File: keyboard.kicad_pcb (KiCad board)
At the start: 2 copper layers, 229.9 x 77.5 mm, 212 parts, among them IC1 ATMEGA32U4, J1 USBMINI_B05, P1 ISP, P2 GPIO Port, Q1 MOS_P, X1 CRYSTAL

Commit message: Final touches on schematic & Clean up PCB
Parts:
- added D321, D331, D381, D41, D42: DIODE, Diodes_SMD:SOD-123, B.Cu at (151.3, 129.9)
- added LED331: LED, mx1a:MX1A-led, F.Cu at (175.3, 143.5)
- added LED341: LED, mx1a:MX1A-led, F.Cu at (146.1, 151.1)
- added LED391: LED, mx1a:MX1A-led, F.Cu at (81.3, 154.9)
- added LED41: LED, mx1a:MX1A-led, F.Cu at (53.3, 170.2)
- added LED42: LED, mx1a:MX1A-led, F.Cu at (199.4, 141.0)
- added LR331, LR341, LR391, LR43: 330R, Resistors_SMD:R_0805, B.Cu at (151.3, 129.9)
- added LR42: 330R, Resistors_SMD:R_0805, B.Cu at (133.3, 130.8)
- added S321: MX1A, mx1a:MX1A, F.Cu at (58.4, 146.1)
- added S331: MX1A, mx1a:MX1A, F.Cu at (108.0, 133.3)
- added S381: MX1A, mx1a:MX1A, F.Cu at (162.6, 165.1)
- added S41: MX1A, mx1a:MX1A, F.Cu at (124.5, 165.1)
- added S42: MX1A, mx1a:MX1A, F.Cu at (94.0, 171.4)
- D1, D10, D11, D12, D13, D14, D15, D16, D17, D18, D19, D2, D20, D21, D22, D23, D24, D25, D26, D27, D28, D29, D3, D30, D31, D32, D33, D34, D35, D36, D37, D38, D39, D4, D40, D5, D6, D7, D8, D9: footprint SM0805:SM0805D -> Diodes_SMD:SOD-123
- IC1: footprint tqfp:TQFP44 -> Housings_QFP:TQFP-44_10x10mm_Pitch0.8mm
- LED1, LED10, LED11, LED12, LED13, LED14, LED15, LED16, LED17, LED18, LED19, LED2, LED20, LED21, LED22, LED23, LED24, LED25, LED26, LED27, LED28, LED29, LED3, LED30, LED31, LED32, LED33, LED34, LED35, LED36, LED37, LED38, LED39, LED4, LED40, LED5, LED6, LED7, LED8, LED9: footprint mx1a-led:MX1A-led -> mx1a:MX1A-led
- S1, S10, S11, S12, S13, S14, S15, S16, S17, S18, S19, S2, S20, S21, S22, S23, S24, S25, S26, S27, S28, S29, S3, S30, S31, S32, S33, S34, S35, S36, S38, S39, S4, S40, S5, S6, S7, S8, S9: footprint MX1A_alps:MX1ALPS -> mx1a:MX1A
- S37: footprint 6.25:CHERRY_PCB_625H_Rev -> mx1a:MX1A
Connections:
- net /Matrix/Col0 renamed /Col0
- net /Matrix/Col1 renamed /Col1
- net /Matrix/Col2 renamed /Col2
- net /Matrix/Col3 renamed /Col3
- net /Matrix/Col6 renamed /Col6
- net /Matrix/Row0 renamed /Row0
- net /Matrix/Row1 renamed /Row1
- net /Matrix/Row2 renamed /Row2
- net /Matrix/Row3 renamed /Row3
- net /led/Backlight renamed /Backlight
- net /led/CapsLock renamed /Caps
- net /led/ESC renamed /ESC
- net /led/WASD renamed /WASD
- D10 pad 1: /Matrix/Col9 -> /Col9
- D11 pad 1: /Matrix/Col10 -> /Col10
- D16 pad 1: /Matrix/Col4 -> /Col4
- D17 pad 1: /Matrix/Col5 -> /Col5
- D19 pad 1: /Matrix/Col7 -> /Col7
- D20 pad 1: /Matrix/Col8 -> /Col8
- D21 pad 1: /Matrix/Col9 -> /Col9
- D22 pad 1: /Matrix/Col10 -> /Col10
- D27 pad 1: /Matrix/Col4 -> /Col4
- D28 pad 1: /Matrix/Col5 -> /Col5
- D30 pad 1: /Matrix/Col7 -> /Col7
- D31 pad 1: /Matrix/Col8 -> /Col8
- D32 pad 1: /Matrix/Col9 -> /Col9
- D33 pad 1: /Matrix/Col10 -> /Col10
- D37 pad 1: /Matrix/Col5 -> /Col4
- D38 pad 1: /Matrix/Col8 -> /Col5
- D39 pad 1: /Matrix/Col9 -> /Col7
- D40 pad 1: /Matrix/Col10 -> /Col8
- D5 pad 1: /Matrix/Col4 -> /Col4
- D6 pad 1: /Matrix/Col5 -> /Col5
- D8 pad 1: /Matrix/Col7 -> /Col7
- D9 pad 1: /Matrix/Col8 -> /Col8
- IC1 pad 12: /Matrix/Col10 -> /Col10
- IC1 pad 28: /Matrix/Col7 -> /Col7
- IC1 pad 29: /Matrix/Col8 -> /Col8
- IC1 pad 30: /Matrix/Col9 -> /Col9
- IC1 pad 32: /led/Bottom -> /Bottom
- IC1 pad 36: /Matrix/Col5 -> /Col5
- IC1 pad 37: /Matrix/Col4 -> /Col4
- LR41 pad 1: Net-(LR41-Pad1) -> /led/LRow0
- LR41 pad 2: /led/Bottom -> Net-(LED41-Pad1)
- RGBLED1 pad 4: Net-(LR41-Pad1) -> Net-(LR43-Pad1)
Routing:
- net GND: track 1231.4 -> 0.00 mm, vias 33 -> 0
- net VCC: track 978.1 -> 0.00 mm, vias 49 -> 0
- net /led/LRow0: track 818.9 -> 0.00 mm, vias 32 -> 0
- net /Row2: track 314.2 -> 0.00 mm, vias 2 -> 0
- net /Row3: track 310.6 -> 0.00 mm, vias 5 -> 0
- net /Row1: track 305.8 -> 0.00 mm, vias 5 -> 0
- net /ESC: track 292.0 -> 0.00 mm, vias 1 -> 0
- net /Matrix/Col10: track 281.1 -> 0.00 mm, vias 9 -> 0
- net /Row0: track 277.7 -> 0.00 mm, vias 2 -> 0
- net /Matrix/Col8: track 235.0 -> 0.00 mm, vias 2 -> 0
- net /Matrix/Col9: track 228.9 -> 0.00 mm, vias 2 -> 0
- net /GPIO2: track 227.9 -> 0.00 mm, vias 6 -> 0
- net /GPIO0: track 206.8 -> 0.00 mm, vias 6 -> 0
- net /GPIO1: track 206.6 -> 0.00 mm, vias 8 -> 0
- net /GPIO3: track 167.0 -> 0.00 mm, vias 3 -> 0
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
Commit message: 旋转跳跃我闭着眼
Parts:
- moved C7 116.7 mm to (255.3, 137.2)
- moved C1 116.6 mm to (255.3, 141.0)
- moved C2 116.6 mm to (255.3, 144.8)
- moved C5 116.5 mm to (255.3, 148.6)
- moved C4 116.1 mm to (224.0, 149.1)
- moved R3 116.1 mm to (228.1, 151.1)
- moved R5 116.1 mm to (245.9, 136.9)
- moved C3 116.1 mm to (228.6, 135.9)
- moved C6 116.1 mm to (224.0, 138.9)
- moved IC1 116.1 mm to (237.0, 145.0)
- moved X1 116.1 mm to (249.7, 143.3)
- moved S37 90.5 mm to (71.5, 135.5)
- moved S321 23.4 mm to (40.6, 130.8), turned to 180 degrees
- moved LR43 6.86 mm to (157.5, 127.0)
- moved D41 3.10 mm to (152.4, 127.0)
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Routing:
- net Net-(C1-Pad1): track 0.00 -> 14.5 mm
- net VCC: track 0.00 -> 9.38 mm
- net Net-(C2-Pad1): track 0.00 -> 7.27 mm
- net /~Res: track 0.00 -> 6.77 mm

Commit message: Layout
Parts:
- removed D321, D331, D381: DIODE, Diodes_SMD:SOD-123
- removed G*** (x2): LOGO, cw40-logo:logo
- removed LR331, LR341, LR391: 330R, Resistors_SMD:R_0805
- removed MXLED (x5): VAL**, holes:PKRHC
- removed S0: DTSM-6, switch:DTSM-6
- added LED371: LED, mx1a-led:MX1A-led, B.Cu at (91.7, 110.2)
- added LED411: LED, mx1a-led:MX1A-led, B.Cu at (232.2, 110.2)
- added MXST: VAL**, mx1a:MXST, F.Cu at (160.8, 110.2)
- added MXST: VAL**, mx1a:MXST, F.Cu at (137.0, 110.2)
- added MXST: VAL**, mx1a:MXST, F.Cu at (184.6, 110.2)
- added MXST: VAL**, mx1a:MXST, F.Cu at (113.2, 110.2)
- added S361: MX1A, mx1a:MX1A, F.Cu at (91.7, 110.2)
- added S401: MX1A, mx1a:MX1A, F.Cu at (232.2, 110.2)
- IC1: footprint Housings_QFP:TQFP-44_10x10mm_Pitch0.8mm -> TQFP44:TQFP44
- LED1, LED10, LED11, LED12, LED13, LED14, LED15, LED16, LED17, LED18, LED19, LED2, LED20, LED21, LED22, LED23, LED24, LED25, LED26, LED27, LED28, LED29, LED3, LED30, LED31, LED32, LED33, LED34, LED35, LED36, LED37, LED38, LED39, LED391, LED4, LED40, LED41, LED42, LED5, LED6, LED7, LED8, LED9: footprint mx1a:MX1A-led -> mx1a-led:MX1A-led
- LED331, LED341: footprint mx1a:MX1A-led -> mx1a-led:MX1A-led; moved to B.Cu
- S38: footprint mx1a:MX1A -> 6.25:CHERRY_PCB_625H_Rev
- moved S42 200.7 mm to (256.0, 53.1)
- moved S321 195.6 mm to (232.2, 91.2)
- moved LED41 186.4 mm to (229.8, 110.2)
- moved LR41 179.4 mm to (237.5, 105.4)
- moved S331 151.7 mm to (253.7, 91.2), turned to 180 degrees
- moved S41 140.4 mm to (253.7, 110.2)
- moved LR42 128.3 mm to (259.1, 105.4), turned to 90 degrees
- moved LED341 123.2 mm to (253.7, 91.2), turned to 0 degrees
- moved D42 121.0 mm to (248.9, 58.4), turned to 270 degrees
- moved LR43 116.2 mm to (61.0, 62.2)
- moved LED391 101.8 mm to (172.7, 110.2)
- moved D41 94.8 mm to (246.4, 114.3), turned to 270 degrees
- moved C1 83.8 mm to (179.1, 106.0)
- moved C2 81.6 mm to (179.1, 115.6), turned to 270 degrees
- moved LED331 77.3 mm to (232.2, 91.2), turned to 0 degrees
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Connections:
- LED331 pad 1: Net-(LED331-Pad1) -> Net-(LED33-Pad1)
- LED341 pad 1: Net-(LED341-Pad1) -> Net-(LED34-Pad1)
- LED391 pad 1: Net-(LED391-Pad1) -> Net-(LED39-Pad1)
- S321 pad 2: Net-(D321-Pad2) -> Net-(D32-Pad2)
- S331 pad 2: Net-(D331-Pad2) -> Net-(D33-Pad2)
- S381 pad 2: Net-(D381-Pad2) -> Net-(D38-Pad2)
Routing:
- net Net-(C1-Pad1): track 14.5 -> 0.00 mm
- net VCC: track 9.38 -> 0.00 mm
- net Net-(C2-Pad1): track 7.27 -> 0.00 mm
- net /~Res: track 6.77 -> 0.00 mm
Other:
- board text removed: "CryptoWall40"
- board text removed: "Special Thanks to SmallFry40"

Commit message: some client
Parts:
- removed LED31: LED, mx1a-led:MX1A-led
- moved C5 109.1 mm to (150.5, 118.0), turned to 180 degrees
- moved C7 107.1 mm to (150.5, 115.0), turned to 180 degrees
- moved R5 102.2 mm to (146.0, 115.0)
- moved P1 95.3 mm to (142.0, 107.5)
- moved C3 89.6 mm to (141.5, 115.0)
- moved C6 85.1 mm to (141.5, 118.0), turned to 180 degrees
- moved C4 84.0 mm to (146.0, 118.0), turned to 180 degrees
- moved C2 20.6 mm to (192.0, 99.5), turned to 0 degrees
- moved R3 20.1 mm to (197.5, 99.5)
- moved LR40 11.0 mm to (215.5, 105.0)
- moved LR32 11.0 mm to (217.5, 87.0)
- moved D31 10.5 mm to (207.5, 86.5)
- moved D38 10.3 mm to (153.5, 105.5)
- moved D39 10.2 mm to (205.0, 105.5)
- moved D40 9.68 mm to (225.0, 106.0)
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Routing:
- net /Row3: track 0.00 -> 281.6 mm
- net Net-(D41-Pad2): track 0.00 -> 17.6 mm, vias 0 -> 2
- net GND: track 0.00 -> 17.1 mm

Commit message: add some client
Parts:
- moved C8 100.5 mm to (136.9, 114.0)
- moved C3 57.5 mm to (197.1, 100.6)
- moved C16 34.5 mm to (168.9, 99.1)
- moved R3 20.2 mm to (188.7, 117.7)
- moved D25 15.0 mm to (103.0, 86.1)
- moved R1 3.76 mm to (57.2, 58.8)
- moved R2 3.73 mm to (54.8, 58.8)
- moved C2 1.08 mm to (192.0, 100.6)
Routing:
- net VCC: track 0.00 -> 42.9 mm, vias 0 -> 4
- net GND: track 17.1 -> 45.3 mm
- net Net-(C2-Pad1): track 0.00 -> 27.1 mm, vias 0 -> 2
- net Net-(C1-Pad1): track 0.00 -> 16.3 mm, vias 0 -> 1
- net Net-(J1-Pad2): track 0.00 -> 14.5 mm
- net Net-(LED12-Pad1): track 0.00 -> 8.48 mm
- net Net-(C3-Pad1): track 0.00 -> 6.43 mm
- net Net-(J1-Pad3): track 0.00 -> 4.07 mm

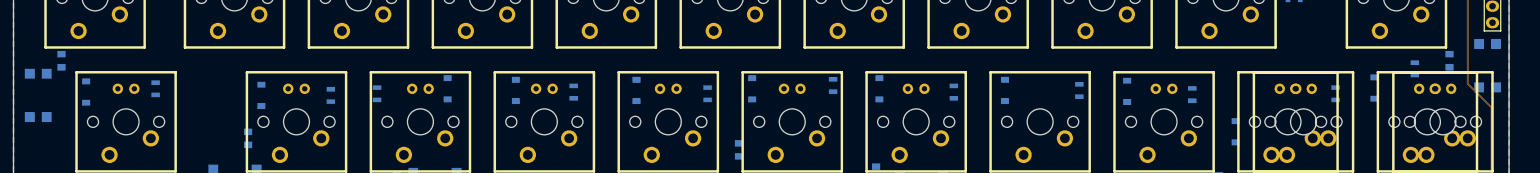
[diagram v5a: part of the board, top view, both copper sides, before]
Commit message: Change RGB led position
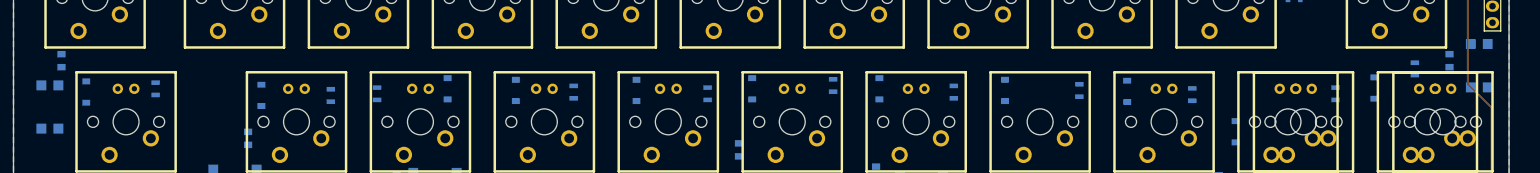
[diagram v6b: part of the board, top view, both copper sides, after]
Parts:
- moved RGBLED12 2.51 mm to (41.9, 88.9), turned to 90 degrees
- moved RGBLED6 1.27 mm to (261.6, 82.5)

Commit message: add holes remove link
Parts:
- added MXLED: HOLE, holes:Mechanical_Hole, F.Cu at (265.7, 95.5)
- added MXLED: HOLE, holes:Mechanical_Hole, F.Cu at (238.8, 63.8)
- added MXLED: HOLE, holes:Mechanical_Hole, F.Cu at (136.9, 80.0)
- added MXLED: HOLE, holes:Mechanical_Hole, F.Cu at (37.6, 97.0)
- added MXLED: HOLE, holes:Mechanical_Hole, F.Cu at (102.4, 114.3)
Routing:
- net /Row3: track 281.6 -> 45.3 mm
- net VCC: track 42.9 -> 1.67 mm, vias 4 -> 0
- net GND: track 45.3 -> 4.83 mm
- net Net-(C2-Pad1): track 27.1 -> 0.00 mm, vias 2 -> 0
- net Net-(C1-Pad1): track 16.3 -> 0.00 mm, vias 1 -> 0
- net Net-(J1-Pad2): track 14.5 -> 0.00 mm
- net Net-(J1-Pad3): track 4.07 -> 0.00 mm

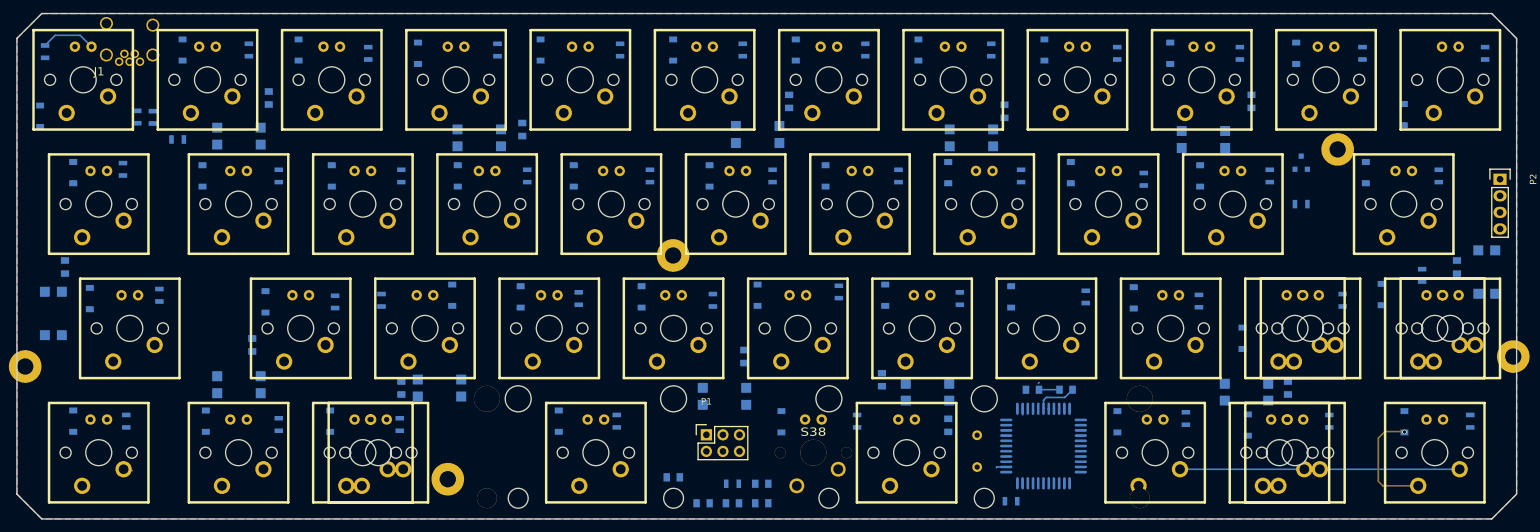
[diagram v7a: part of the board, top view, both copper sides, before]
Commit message: 手工布线完成
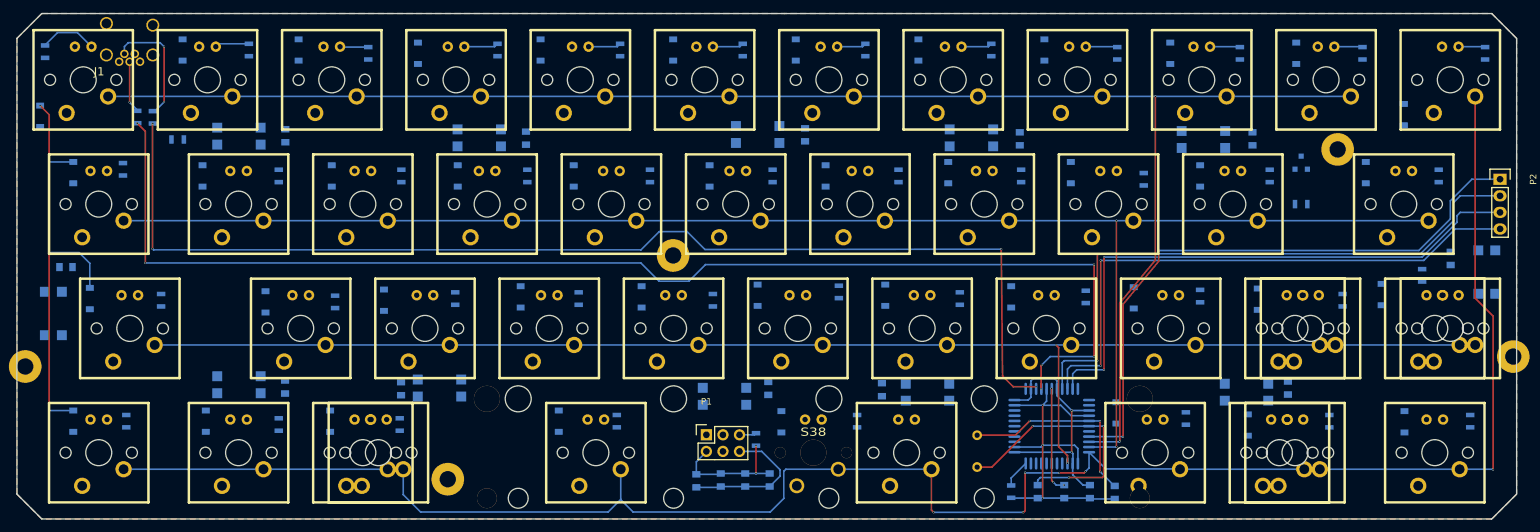
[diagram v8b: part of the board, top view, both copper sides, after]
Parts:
- added LED31: LED, mx1a-led:MX1A-led, F.Cu at (194.1, 91.2)
- moved C14 184.2 mm to (256.1, 80.5), turned to 90 degrees
- moved C17 109.4 mm to (151.5, 100.4)
- moved C20 73.1 mm to (43.8, 81.8), turned to 180 degrees
- moved C8 63.9 mm to (200.8, 116.2), turned to 270 degrees
- moved C18 52.9 mm to (95.2, 100.4)
- moved C10 40.7 mm to (114.4, 62.0), turned to 90 degrees
- moved C13 37.0 mm to (225.7, 62.1)
- moved C12 36.0 mm to (190.0, 62.1), turned to 90 degrees
- moved C11 30.8 mm to (157.1, 61.5)
- moved C1 27.5 mm to (204.6, 116.3)
- moved C19 17.8 mm to (77.4, 100.2)
- moved C2 15.6 mm to (192.8, 116.2), turned to 270 degrees
- moved C3 15.6 mm to (196.8, 116.2), turned to 270 degrees
- moved LR26 11.3 mm to (103.5, 86.6)
- moved D25 10.5 mm to (92.6, 86.9)
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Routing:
- net /Row3: track 45.3 -> 298.5 mm, vias 0 -> 7
- net /Row0: track 0.00 -> 250.1 mm, vias 0 -> 2
- net /Row1: track 0.00 -> 238.9 mm, vias 0 -> 3
- net /Row2: track 0.00 -> 221.3 mm, vias 0 -> 2
- net Net-(IC1-Pad4): track 0.00 -> 196.0 mm, vias 0 -> 6
- net Net-(IC1-Pad3): track 0.00 -> 177.3 mm, vias 0 -> 4
- net /GPIO3: track 0.00 -> 94.3 mm, vias 0 -> 2
- net /GPIO2: track 0.00 -> 92.9 mm, vias 0 -> 2
- net /GPIO0: track 0.00 -> 89.5 mm, vias 0 -> 2
- net /GPIO1: track 0.00 -> 87.7 mm, vias 0 -> 2
- net GND: track 4.83 -> 80.1 mm, vias 0 -> 3
- net /Col0: track 0.00 -> 65.3 mm, vias 0 -> 4
- net VCC: track 1.67 -> 59.2 mm, vias 0 -> 4
- net Net-(C2-Pad1): track 0.00 -> 40.8 mm, vias 0 -> 3
- net Net-(C1-Pad1): track 0.00 -> 30.7 mm, vias 0 -> 3
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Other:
- net class Default: via_dia 0.6 -> 0.3; via_drill 0.4 -> 0.25
- rule via_min_drill: 0.3 -> 0.1
- rule via_min_size: 0.4 -> 0.1
